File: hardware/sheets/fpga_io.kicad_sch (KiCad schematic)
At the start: 1 part, among them U1 A3CZ065BB18AE7S

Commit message: Remove dangling track stubs; No-Connect flag from B3 to C2
- Deleted the 6 dangling stubs DRC reported and the dead-end branches behind
  them: an unused PG_0V75 route on L4 at U3, an abandoned PG_1V8 route on
  B.Cu (83.1, 111.3) to (90.75, 104.14), and short stubs on CUK_CS, +1V8,
  HR_DQ7 and +1V2_RCORE. DRC stayed at 0 unconnected after each deletion.
- fpga_io: the No-Connect flag on U1 B3 (now HR_RESET_N) moved to the unused C2.

DRC: 0 errors, 0 unconnected, 0 parity issues; silkscreen warnings only.
ERC: only GNDSENSE on VCC_SENSE_N (intended).

Co-Authored-By: Claude Opus 5.5 <noreply@anthropic.com>
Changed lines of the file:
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@@
 	)
 	(no_connect
-		(at 342.9 63.5)
+		(at 342.9 68.58)
 	)
 	(no_connect

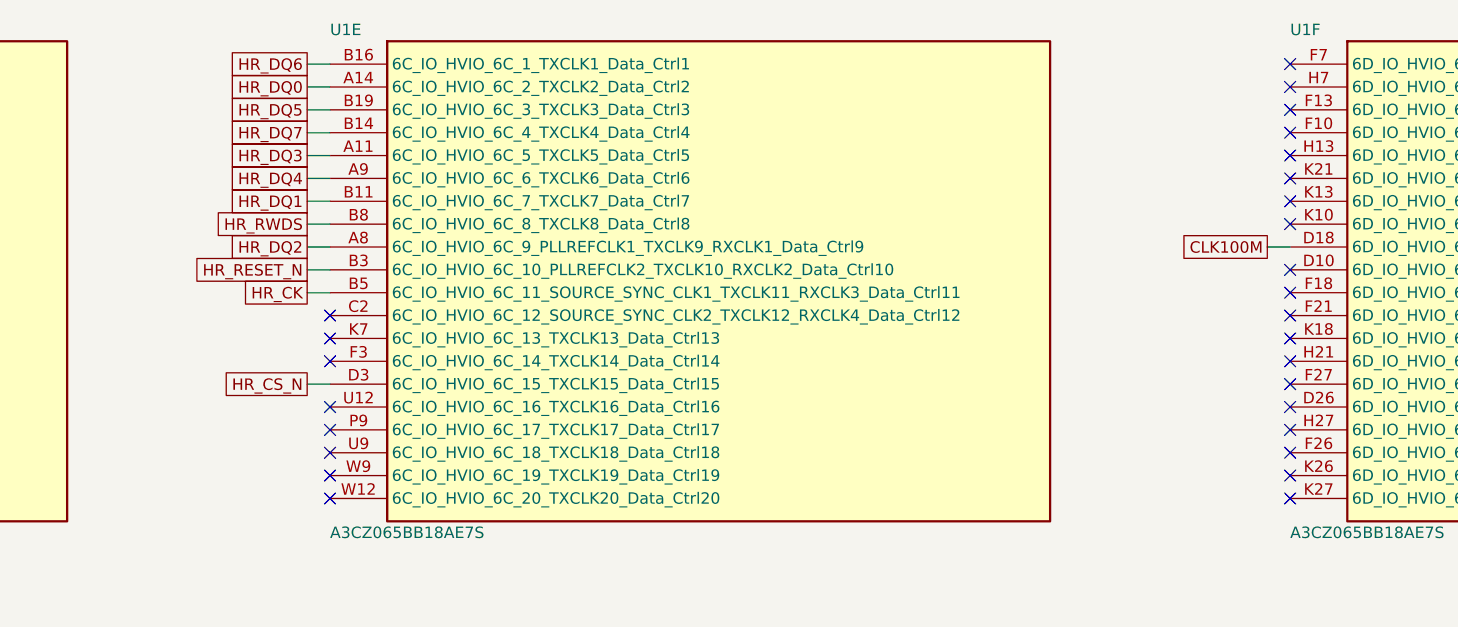
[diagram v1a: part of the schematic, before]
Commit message: HyperRAM to bank 6D; BGA via-in-pads 0.25/0.15; Default via 0.3/0.15
- Schematic: the 12 HyperRAM signals moved from bank 6C to 6D for easier
  length matching: HR_CK F18 (SOURCE_SYNC_CLK1), CS_N H7, RWDS F10,
  RESET_N F7, DQ0-7 F21 H21 D10 H13 F13 F27 D26 F26. 6D is 1.8 V on
  +1V8_HR and keeps CLK100M on D18; 6C is now unused (No-Connect flags).
  pin_assignment.csv / io_assignment.csv regenerated; docs updated.
- Board: PCB updated from the schematic (HyperRAM reroute in progress);
  ten oversized 0.35/0.2 vias in BGA/0201 pads (incl. U1 D7) reset to
  0.25/0.15 so tracks fit between the balls.
- Default net class via 0.35/0.2 -> 0.3/0.15.

DRC: no clearance errors; 8 unconnected and 9 dangling items, all on the
HyperRAM nets being rerouted.

Co-Authored-By: Claude Opus 5.5 <noreply@anthropic.com>
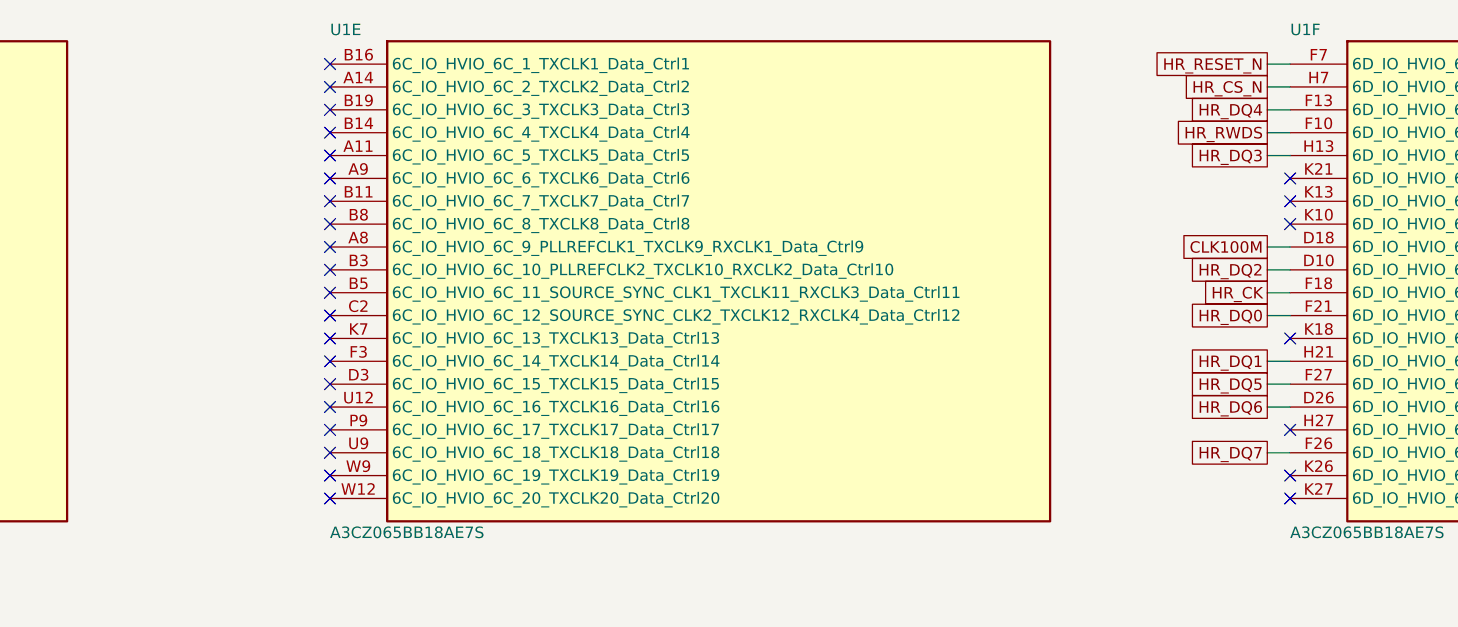
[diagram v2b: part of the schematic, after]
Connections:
- net HR_CK: now also U1.F18 (6D_IO_HVIO_6D_11_SOURCE_SYNC_CLK1_TXCLK11_RXCLK3_Data_Ctrl11); no longer U1.B5 (6C_IO_HVIO_6C_11_SOURCE_SYNC_CLK1_TXCLK11_RXCLK3_Data_Ctrl11)
- net HR_CS_N: now also U1.H7 (6D_IO_HVIO_6D_2_TXCLK2_Data_Ctrl2); no longer U1.D3 (6C_IO_HVIO_6C_15_TXCLK15_Data_Ctrl15)
- net HR_DQ0: now also U1.F21 (6D_IO_HVIO_6D_12_SOURCE_SYNC_CLK2_TXCLK12_RXCLK4_Data_Ctrl12); no longer U1.A14 (6C_IO_HVIO_6C_2_TXCLK2_Data_Ctrl2)
- net HR_DQ1: now also U1.H21 (6D_IO_HVIO_6D_14_TXCLK14_Data_Ctrl14); no longer U1.B11 (6C_IO_HVIO_6C_7_TXCLK7_Data_Ctrl7)
- net HR_DQ2: now also U1.D10 (6D_IO_HVIO_6D_10_PLLREFCLK2_TXCLK10_RXCLK2_Data_Ctrl10); no longer U1.A8 (6C_IO_HVIO_6C_9_PLLREFCLK1_TXCLK9_RXCLK1_Data_Ctrl9)
- net HR_DQ3: now also U1.H13 (6D_IO_HVIO_6D_5_TXCLK5_Data_Ctrl5); no longer U1.A11 (6C_IO_HVIO_6C_5_TXCLK5_Data_Ctrl5)
- net HR_DQ4: now also U1.F13 (6D_IO_HVIO_6D_3_TXCLK3_Data_Ctrl3); no longer U1.A9 (6C_IO_HVIO_6C_6_TXCLK6_Data_Ctrl6)
- net HR_DQ5: now also U1.F27 (6D_IO_HVIO_6D_15_TXCLK15_Data_Ctrl15); no longer U1.B19 (6C_IO_HVIO_6C_3_TXCLK3_Data_Ctrl3)
- net HR_DQ6: now also U1.D26 (6D_IO_HVIO_6D_16_TXCLK16_Data_Ctrl16); no longer U1.B16 (6C_IO_HVIO_6C_1_TXCLK1_Data_Ctrl1)
- net HR_DQ7: now also U1.F26 (6D_IO_HVIO_6D_18_TXCLK18_Data_Ctrl18); no longer U1.B14 (6C_IO_HVIO_6C_4_TXCLK4_Data_Ctrl4)
- net HR_RESET_N: now also U1.F7 (6D_IO_HVIO_6D_1_TXCLK1_Data_Ctrl1); no longer U1.B3 (6C_IO_HVIO_6C_10_PLLREFCLK2_TXCLK10_RXCLK2_Data_Ctrl10)
- net HR_RWDS: now also U1.F10 (6D_IO_HVIO_6D_4_TXCLK4_Data_Ctrl4); no longer U1.B8 (6C_IO_HVIO_6C_8_TXCLK8_Data_Ctrl8)
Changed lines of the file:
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@@
 	)
 	(no_connect
-		(at 449.58 40.64)
+		(at 342.9 63.5)
 	)
 	(no_connect
@@
 	)
 	(no_connect
-		(at 449.58 83.82)
+		(at 342.9 48.26)
 	)
 	(no_connect
@@
 	)
 	(no_connect
-		(at 449.58 76.2)
+		(at 342.9 45.72)
 	)
 	(no_connect
@@
 	)
 	(no_connect
-		(at 449.58 63.5)
+		(at 342.9 60.96)
 	)
 	(no_connect
@@
 	)
 	(no_connect
-		(at 449.58 50.8)
+		(at 342.9 50.8)
 	)
 	(no_connect
@@
 	)
 	(no_connect
-		(at 449.58 73.66)
+		(at 342.9 55.88)
 	)
 	(no_connect
@@
 	)
 	(no_connect
-		(at 449.58 68.58)
-	)
-	(no_connect
-		(at 449.58 78.74)
+		(at 342.9 43.18)
+	)
+	(no_connect
+		(at 342.9 40.64)
 	)
 	(no_connect
@@
 	)
 	(no_connect
-		(at 449.58 66.04)
+		(at 342.9 66.04)
 	)
 	(no_connect
@@
 	)
 	(no_connect
-		(at 449.58 48.26)
-	)
-	(no_connect
-		(at 449.58 45.72)
+		(at 342.9 58.42)
+	)
+	(no_connect
+		(at 342.9 53.34)
 	)
 	(no_connect
@@
 	)
 	(no_connect
-		(at 449.58 43.18)
+		(at 342.9 76.2)
 	)
 	(no_connect
@@
 	(wire
 		(pts
-			(xy 340.36 63.5) (xy 342.9 63.5)
+			(xy 447.04 40.64) (xy 449.58 40.64)
 		)
 		(stroke
@@
 	(wire
 		(pts
-			(xy 340.36 40.64) (xy 342.9 40.64)
+			(xy 447.04 78.74) (xy 449.58 78.74)
 		)
 		(stroke
@@
 	(wire
 		(pts
-			(xy 340.36 55.88) (xy 342.9 55.88)
+			(xy 447.04 73.66) (xy 449.58 73.66)
 		)
 		(stroke
@@
 	(wire
 		(pts
-			(xy 342.9 60.96) (xy 340.36 60.96)
-		)
-		(stroke
-			(width 0)
-			(type default)
-		)
-	)
-	(wire
-		(pts
-			(xy 342.9 53.34) (xy 340.36 53.34)
+			(xy 449.58 63.5) (xy 447.04 63.5)
+		)
+		(stroke
+			(width 0)
+			(type default)
+		)
+	)
+	(wire
+		(pts
+			(xy 449.58 45.72) (xy 447.04 45.72)
 		)
 		(stroke
@@
 	(wire
 		(pts
-			(xy 340.36 48.26) (xy 342.9 48.26)
+			(xy 447.04 83.82) (xy 449.58 83.82)
 		)
 		(stroke
@@
 	(wire
 		(pts
-			(xy 342.9 58.42) (xy 340.36 58.42)
+			(xy 449.58 48.26) (xy 447.04 48.26)
 		)
 		(stroke
@@
 	(wire
 		(pts
-			(xy 342.9 50.8) (xy 340.36 50.8)
+			(xy 449.58 50.8) (xy 447.04 50.8)
 		)
 		(stroke
@@
 	(wire
 		(pts
-			(xy 342.9 76.2) (xy 340.36 76.2)
+			(xy 449.58 43.18) (xy 447.04 43.18)
 		)
 		(stroke
@@
 	(wire
 		(pts
-			(xy 342.9 45.72) (xy 340.36 45.72)
+			(xy 449.58 76.2) (xy 447.04 76.2)
 		)
 		(stroke
@@
 	(wire
 		(pts
-			(xy 340.36 43.18) (xy 342.9 43.18)
+			(xy 447.04 68.58) (xy 449.58 68.58)
 		)
 		(stroke
@@
 	(wire
 		(pts
-			(xy 342.9 66.04) (xy 340.36 66.04)
+			(xy 449.58 66.04) (xy 447.04 66.04)
 		)
 		(stroke
@@
 	(global_label "HR_DQ3"
 		(shape passive)
-		(at 340.36 50.8 180)
-		(fields_autoplaced yes)
-		(effects
-			(font
-				(size 1.27 1.27)
-			)
-			(justify right)
-		)
-		(property "Intersheetrefs" "${INTERSHEET_REFS}"
-			(at 340.36 50.8 0)
+		(at 447.04 50.8 180)
+		(fields_autoplaced yes)
+		(effects
+			(font
+				(size 1.27 1.27)
+			)
+			(justify right)
+		)
+		(property "Intersheetrefs" "${INTERSHEET_REFS}"
+			(at 447.04 50.8 0)
 			(hide yes)
 			(show_name no)
@@
 	(global_label "HR_DQ5"
 		(shape passive)
-		(at 340.36 45.72 180)
-		(fields_autoplaced yes)
-		(effects
-			(font
-				(size 1.27 1.27)
-			)
-			(justify right)
-		)
-		(property "Intersheetrefs" "${INTERSHEET_REFS}"
-			(at 340.36 45.72 0)
+		(at 447.04 76.2 180)
+		(fields_autoplaced yes)
+		(effects
+			(font
+				(size 1.27 1.27)
+			)
+			(justify right)
+		)
+		(property "Intersheetrefs" "${INTERSHEET_REFS}"
+			(at 447.04 76.2 0)
 			(hide yes)
 			(show_name no)
@@
 	(global_label "HR_DQ2"
 		(shape passive)
-		(at 340.36 60.96 180)
-		(fields_autoplaced yes)
-		(effects
-			(font
-				(size 1.27 1.27)
-			)
-			(justify right)
-		)
-		(property "Intersheetrefs" "${INTERSHEET_REFS}"
-			(at 340.36 60.96 0)
+		(at 447.04 63.5 180)
+		(fields_autoplaced yes)
+		(effects
+			(font
+				(size 1.27 1.27)
+			)
+			(justify right)
+		)
+		(property "Intersheetrefs" "${INTERSHEET_REFS}"
+			(at 447.04 63.5 0)
 			(hide yes)
 			(show_name no)
@@
 	(global_label "HR_DQ7"
 		(shape passive)
-		(at 340.36 48.26 180)
-		(fields_autoplaced yes)
-		(effects
-			(font
-				(size 1.27 1.27)
-			)
-			(justify right)
-		)
-		(property "Intersheetrefs" "${INTERSHEET_REFS}"
-			(at 340.36 48.26 0)
+		(at 447.04 83.82 180)
+		(fields_autoplaced yes)
+		(effects
+			(font
+				(size 1.27 1.27)
+			)
+			(justify right)
+		)
+		(property "Intersheetrefs" "${INTERSHEET_REFS}"
+			(at 447.04 83.82 0)
 			(hide yes)
 			(show_name no)
@@
 	(global_label "HR_DQ1"
 		(shape passive)
-		(at 340.36 55.88 180)
-		(fields_autoplaced yes)
-		(effects
-			(font
-				(size 1.27 1.27)
-			)
-			(justify right)
-		)
-		(property "Intersheetrefs" "${INTERSHEET_REFS}"
-			(at 340.36 55.88 0)
+		(at 447.04 73.66 180)
+		(fields_autoplaced yes)
+		(effects
+			(font
+				(size 1.27 1.27)
+			)
+			(justify right)
+		)
+		(property "Intersheetrefs" "${INTERSHEET_REFS}"
+			(at 447.04 73.66 0)
 			(hide yes)
 			(show_name no)
@@
 	(global_label "HR_CS_N"
 		(shape passive)
-		(at 340.36 76.2 180)
-		(fields_autoplaced yes)
-		(effects
-			(font
-				(size 1.27 1.27)
-			)
-			(justify right)
-		)
-		(property "Intersheetrefs" "${INTERSHEET_REFS}"
-			(at 340.36 76.2 0)
+		(at 447.04 43.18 180)
+		(fields_autoplaced yes)
+		(effects
+			(font
+				(size 1.27 1.27)
+			)
+			(justify right)
+		)
+		(property "Intersheetrefs" "${INTERSHEET_REFS}"
+			(at 447.04 43.18 0)
 			(hide yes)
 			(show_name no)
@@
 	(global_label "HR_DQ6"
 		(shape passive)
-		(at 340.36 40.64 180)
-		(fields_autoplaced yes)
-		(effects
-			(font
-				(size 1.27 1.27)
-			)
-			(justify right)
-		)
-		(property "Intersheetrefs" "${INTERSHEET_REFS}"
-			(at 340.36 40.64 0)
+		(at 447.04 78.74 180)
+		(fields_autoplaced yes)
+		(effects
+			(font
+				(size 1.27 1.27)
+			)
+			(justify right)
+		)
+		(property "Intersheetrefs" "${INTERSHEET_REFS}"
+			(at 447.04 78.74 0)
 			(hide yes)
 			(show_name no)
@@
 	(global_label "HR_RWDS"
 		(shape passive)
-		(at 340.36 58.42 180)
-		(fields_autoplaced yes)
-		(effects
-			(font
-				(size 1.27 1.27)
-			)
-			(justify right)
-		)
-		(property "Intersheetrefs" "${INTERSHEET_REFS}"
-			(at 340.36 58.42 0)
+		(at 447.04 48.26 180)
+		(fields_autoplaced yes)
+		(effects
+			(font
+				(size 1.27 1.27)
+			)
+			(justify right)
+		)
+		(property "Intersheetrefs" "${INTERSHEET_REFS}"
+			(at 447.04 48.26 0)
 			(hide yes)
 			(show_name no)
@@
 	(global_label "HR_CK"
 		(shape passive)
-		(at 340.36 66.04 180)
-		(fields_autoplaced yes)
-		(effects
-			(font
-				(size 1.27 1.27)
-			)
-			(justify right)
-		)
-		(property "Intersheetrefs" "${INTERSHEET_REFS}"
-			(at 340.36 66.04 0)
+		(at 447.04 66.04 180)
+		(fields_autoplaced yes)
+		(effects
+			(font
+				(size 1.27 1.27)
+			)
+			(justify right)
+		)
+		(property "Intersheetrefs" "${INTERSHEET_REFS}"
+			(at 447.04 66.04 0)
 			(hide yes)
 			(show_name no)
@@
 	(global_label "HR_RESET_N"
 		(shape passive)
-		(at 340.36 63.5 180)
-		(fields_autoplaced yes)
-		(effects
-			(font
-				(size 1.27 1.27)
-			)
-			(justify right)
-		)
-		(property "Intersheetrefs" "${INTERSHEET_REFS}"
-			(at 340.36 63.5 0)
+		(at 447.04 40.64 180)
+		(fields_autoplaced yes)
+		(effects
+			(font
+				(size 1.27 1.27)
+			)
+			(justify right)
+		)
+		(property "Intersheetrefs" "${INTERSHEET_REFS}"
+			(at 447.04 40.64 0)
 			(hide yes)
 			(show_name no)
@@
 	(global_label "HR_DQ0"
 		(shape passive)
-		(at 340.36 43.18 180)
-		(fields_autoplaced yes)
-		(effects
-			(font
-				(size 1.27 1.27)
-			)
-			(justify right)
-		)
-		(property "Intersheetrefs" "${INTERSHEET_REFS}"
-			(at 340.36 43.18 0)
+		(at 447.04 68.58 180)
+		(fields_autoplaced yes)
+		(effects
+			(font
+				(size 1.27 1.27)
+			)
+			(justify right)
+		)
+		(property "Intersheetrefs" "${INTERSHEET_REFS}"
+			(at 447.04 68.58 0)
 			(hide yes)
 			(show_name no)
@@
 	(global_label "HR_DQ4"
 		(shape passive)
-		(at 340.36 53.34 180)
-		(fields_autoplaced yes)
-		(effects
-			(font
-				(size 1.27 1.27)
-			)
-			(justify right)
-		)
-		(property "Intersheetrefs" "${INTERSHEET_REFS}"
-			(at 340.36 53.34 0)
-			(hide yes)
-			(show_name no)
+		(at 447.04 45.72 180)
+		(fields_autoplaced yes)
+		(effects
+			(font
+				(size 1.27 1.27)
+			)
+			(justify right)
+		)
+		(property "Intersheetrefs" "${INTERSHEET_REFS}"
+			(at 447.04 45.72 0)
+			(hide yes)
+			(show_name no)
